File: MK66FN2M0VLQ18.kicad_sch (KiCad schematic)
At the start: 14 parts, among them U1 MK66FN2M0VLQ18, Y1 32.768khz

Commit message: da
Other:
- company: (none) -> TampanTech
- title: (none) -> MicroController
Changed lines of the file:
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@@
 	(generator_version "8.0")
 	(paper "A4")
+	(title_block
+		(title "MicroController")
+		(date "2024-09-08")
+		(rev "1")
+		(company "TampanTech")
+		(comment 1 "Drone Flight Management Unit")
+	)
 	(junction
 		(at 87.63 151.13)

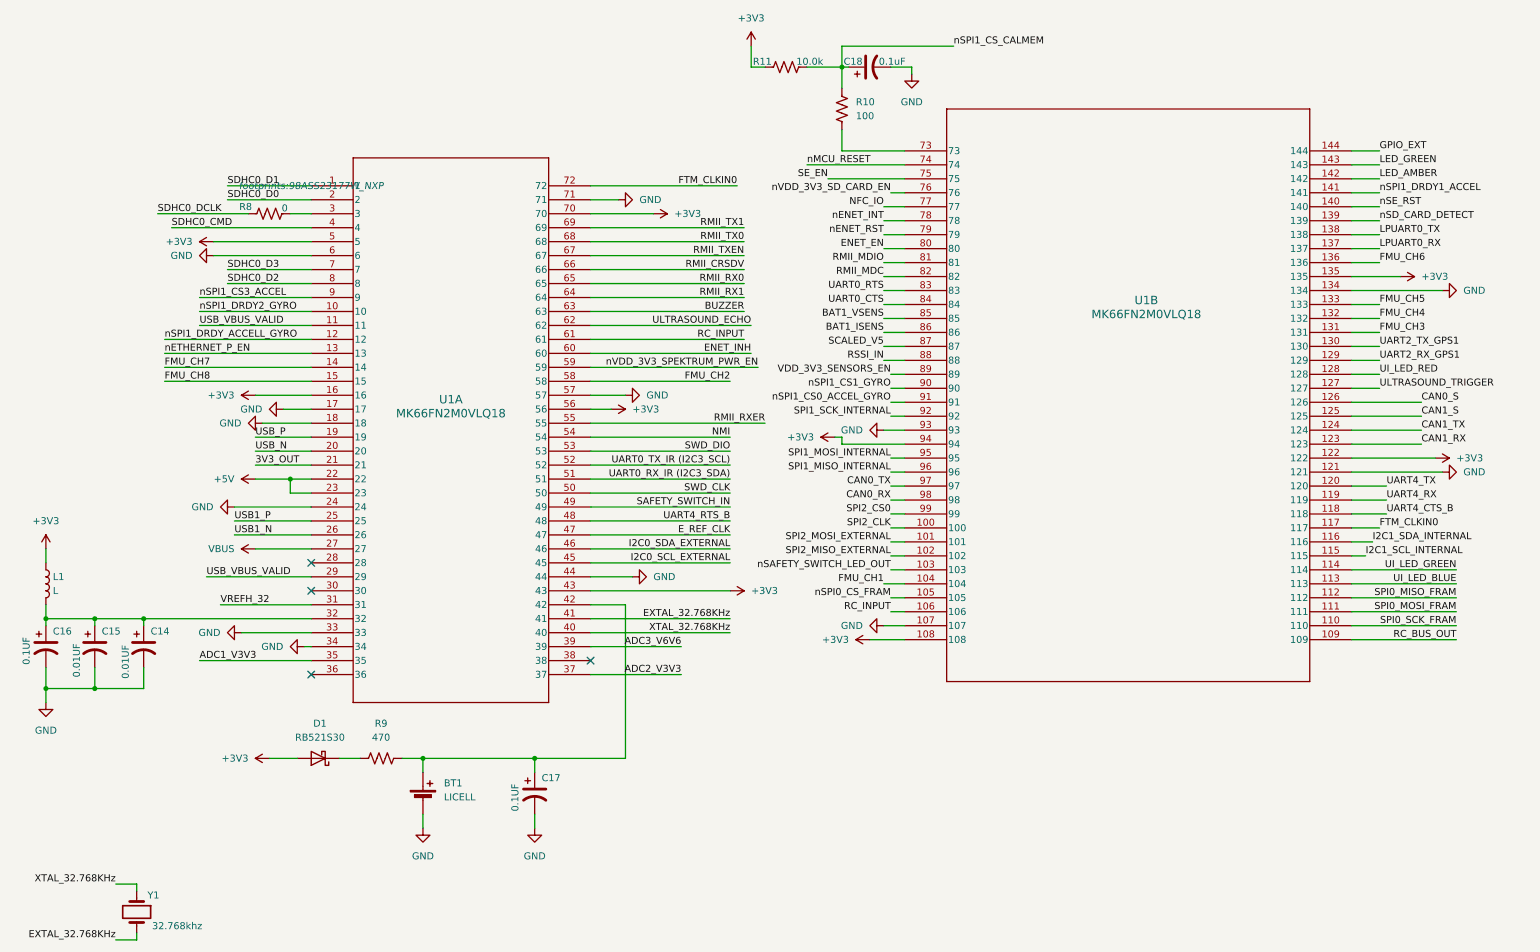
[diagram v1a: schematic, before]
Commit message: change label to global
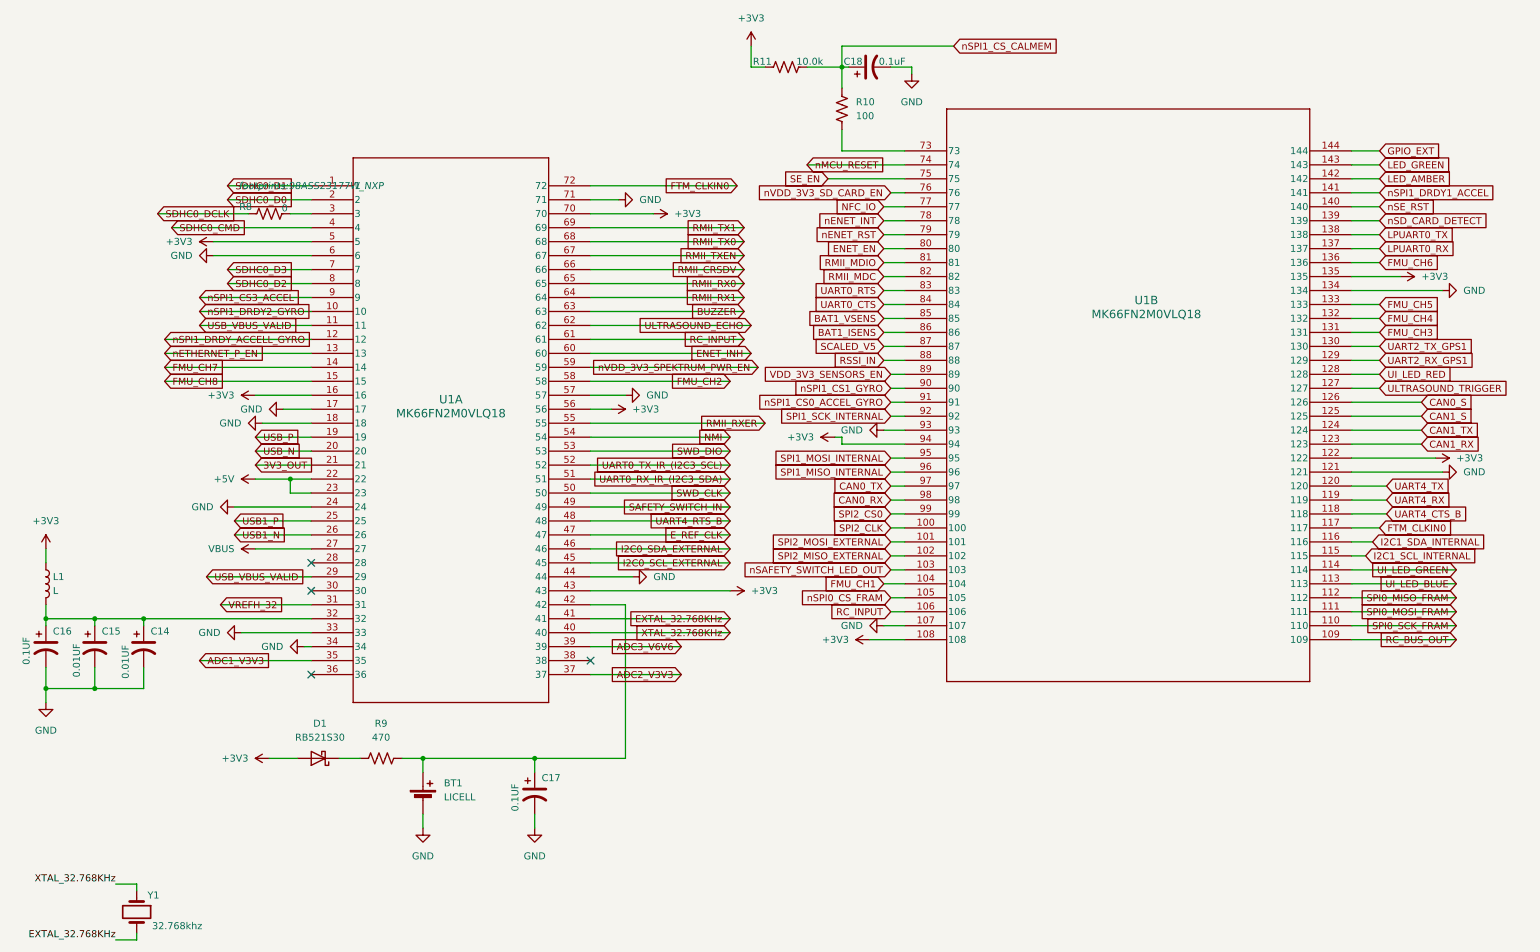
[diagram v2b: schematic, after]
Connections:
- net UART0_RX_IR (I2C3_SDA) renamed UART0_RX_IR_(I2C3_SDA)
- net UART0_TX_IR (I2C3_SCL) renamed UART0_TX_IR_(I2C3_SCL)

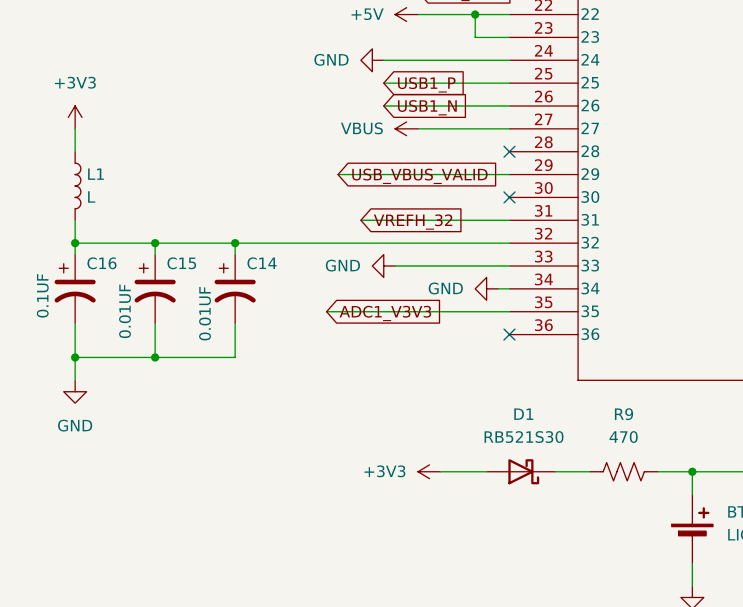
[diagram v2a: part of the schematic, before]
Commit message: change label to global
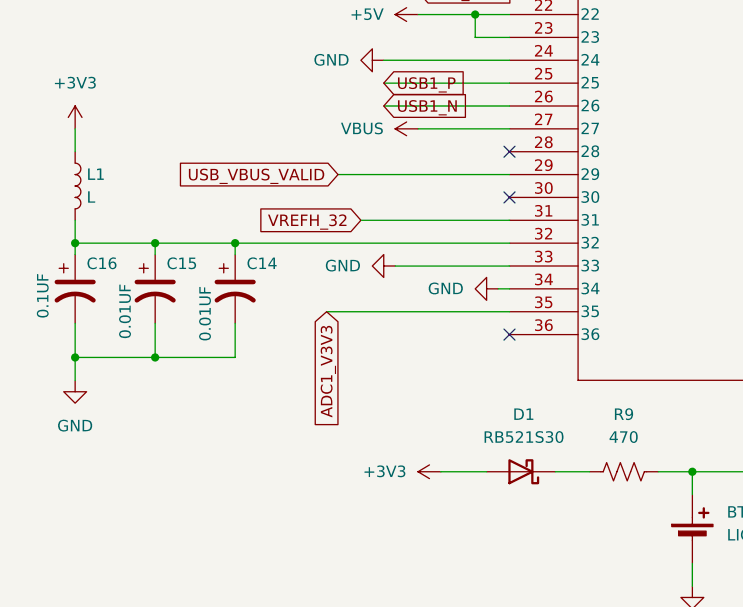
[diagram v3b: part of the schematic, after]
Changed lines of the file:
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@@
 	(global_label "ADC1_V3V3"
 		(shape input)
-		(at 46.99 133.35 0)
-		(fields_autoplaced yes)
-		(effects
-			(font
-				(size 1.27 1.27)
-			)
-			(justify left)
-		)
-		(property "Intersheetrefs" "${INTERSHEET_REFS}"
-			(at 60.3771 133.35 0)
-			(effects
-				(font
-					(size 1.27 1.27)
-				)
-				(justify left)
+		(at 46.99 133.35 270)
+		(fields_autoplaced yes)
+		(effects
+			(font
+				(size 1.27 1.27)
+			)
+			(justify right)
+		)
+		(property "Intersheetrefs" "${INTERSHEET_REFS}"
+			(at 46.99 146.7371 90)
+			(effects
+				(font
+					(size 1.27 1.27)
+				)
+				(justify right)
 				(hide yes)
 			)
@@
 	(global_label "VREFH_32"
 		(shape input)
-		(at 50.8 123.19 0)
-		(fields_autoplaced yes)
-		(effects
-			(font
-				(size 1.27 1.27)
-			)
-			(justify left)
-		)
-		(property "Intersheetrefs" "${INTERSHEET_REFS}"
-			(at 63.0985 123.19 0)
-			(effects
-				(font
-					(size 1.27 1.27)
-				)
-				(justify left)
+		(at 50.8 123.19 180)
+		(fields_autoplaced yes)
+		(effects
+			(font
+				(size 1.27 1.27)
+			)
+			(justify right)
+		)
+		(property "Intersheetrefs" "${INTERSHEET_REFS}"
+			(at 38.5015 123.19 0)
+			(effects
+				(font
+					(size 1.27 1.27)
+				)
+				(justify right)
 				(hide yes)
 			)
@@
 	(global_label "USB_VBUS_VALID"
 		(shape input)
-		(at 48.26 118.11 0)
-		(fields_autoplaced yes)
-		(effects
-			(font
-				(size 1.27 1.27)
-			)
-			(justify left)
-		)
-		(property "Intersheetrefs" "${INTERSHEET_REFS}"
-			(at 66.9691 118.11 0)
-			(effects
-				(font
-					(size 1.27 1.27)
-				)
-				(justify left)
-				(hide yes)
-			)
+		(at 48.26 118.11 180)
+		(fields_autoplaced yes)
+		(effects
+			(font
+				(size 1.27 1.27)
+			)
+			(justify right)
+		)
+		(property "Intersheetrefs" "${INTERSHEET_REFS}"
+			(at 29.5509 118.11 0)
+			(effects
+				(font
+					(size 1.27 1.27)
+				)
+				(justify right)
+				(hide yes)
+			)
